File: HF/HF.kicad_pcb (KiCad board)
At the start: 2 copper layers, 105 x 58 mm, 11 parts, among them J1 SpeakON_NL4, J2 SpeakON_NL4, U1 1+, U2 1-, U3 HF-, U4 HF+

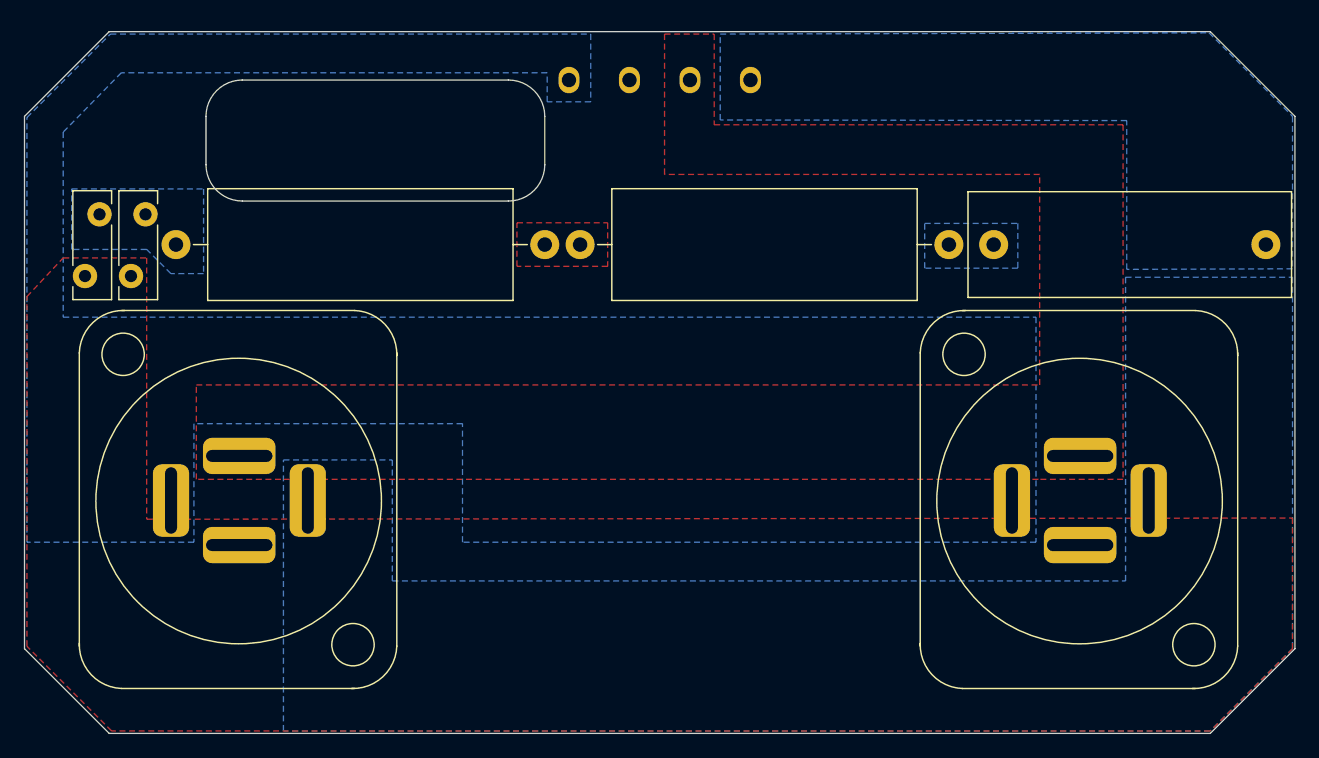
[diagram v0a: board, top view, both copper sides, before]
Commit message: added everything but the inductor
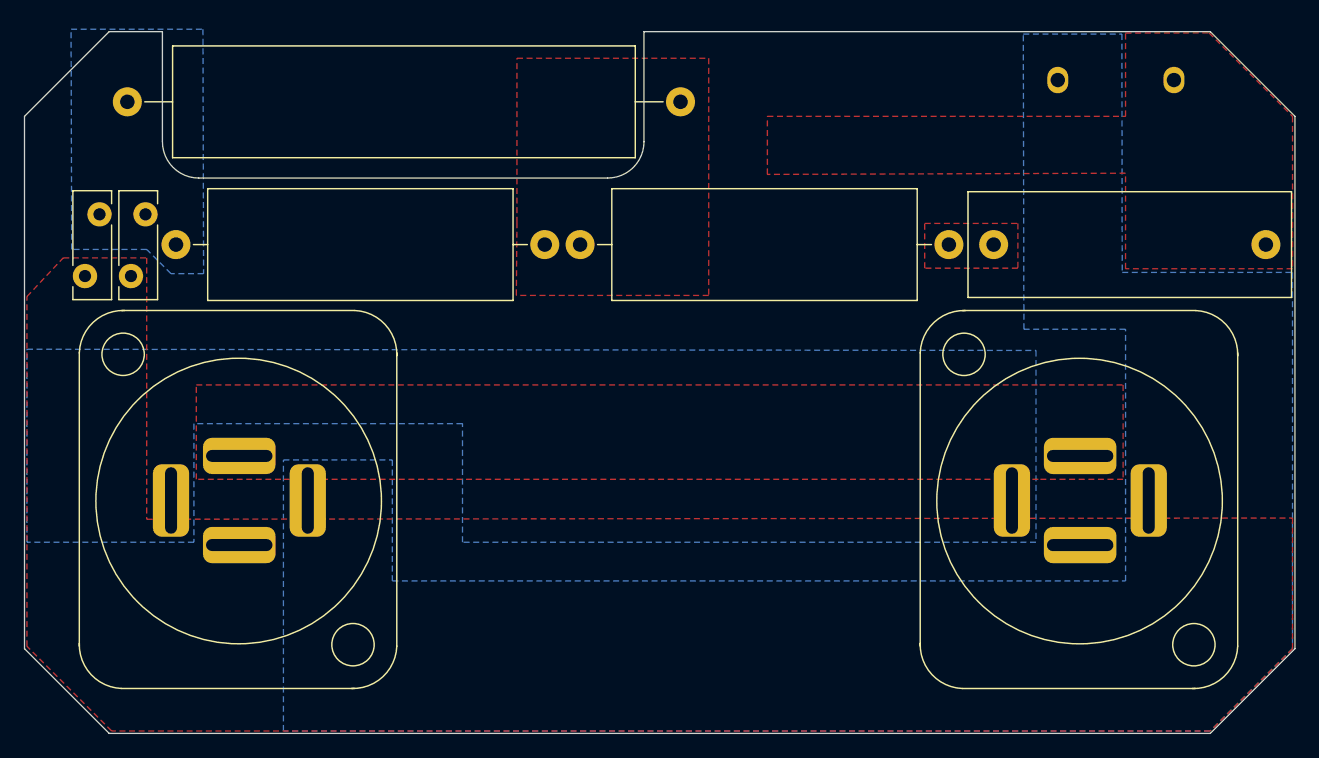
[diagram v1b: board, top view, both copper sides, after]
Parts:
- removed U1: 1+, SpeakON:Reoforo
- removed U2: 1-, SpeakON:Reoforo
- added LA1: 1,5Ω, Resistor_THT:R_Axial_Power_L38.0mm_W9.0mm_P45.72mm, F.Cu at (28.5, 25.8)
- moved U4 35.4 mm to (105.4, 24.0)
- moved U3 35.0 mm to (115.0, 24.0)
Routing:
- added copper zone on F.Cu, net Net-(C1-Pad1)
- added copper zone on F.Cu, net Net-(C1-Pad2)
- removed copper zone on B.Cu, net Net-(C1-Pad1)
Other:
- outline, holes or cut-outs redrawn

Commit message: inductor added
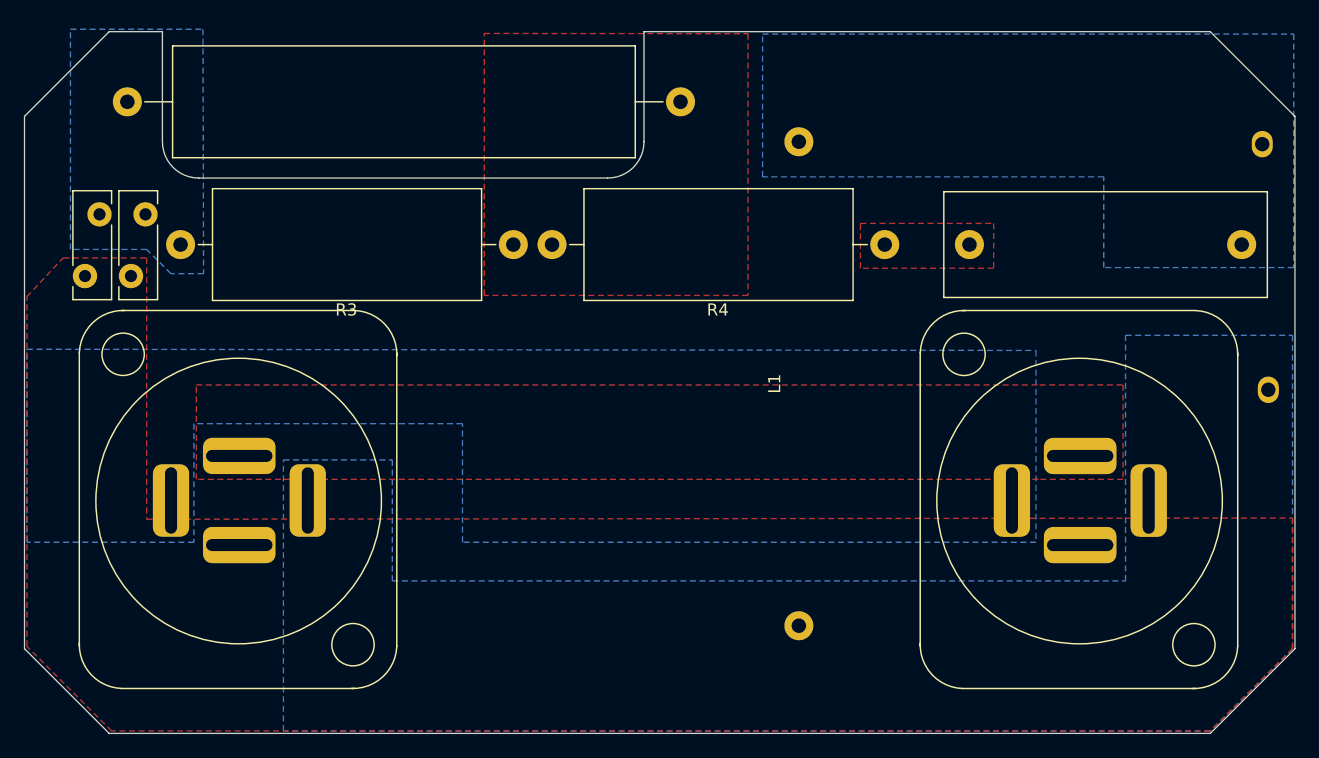
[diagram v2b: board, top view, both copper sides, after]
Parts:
- added L1: 290uH, RES:inductor_40mm, F.Cu at (80.0, 49.1)
- R3, R4: footprint Resistor_THT:R_Axial_Power_L25.0mm_W9.0mm_P30.48mm -> RES:resistor_P27.50mm
- moved U4 31.0 mm to (122.8, 49.6)
- moved U3 9.02 mm to (122.3, 29.3)
- moved R4 5.30 mm to (91.1, 37.6)
- moved R3 2.60 mm to (60.4, 37.6)
- moved C1 2.00 mm to (120.6, 37.6)
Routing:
- added copper zone on B.Cu, net Net-(C1-Pad1)
- removed copper zone on F.Cu, net Net-(C1-Pad1)

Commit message: updated speakON footprint
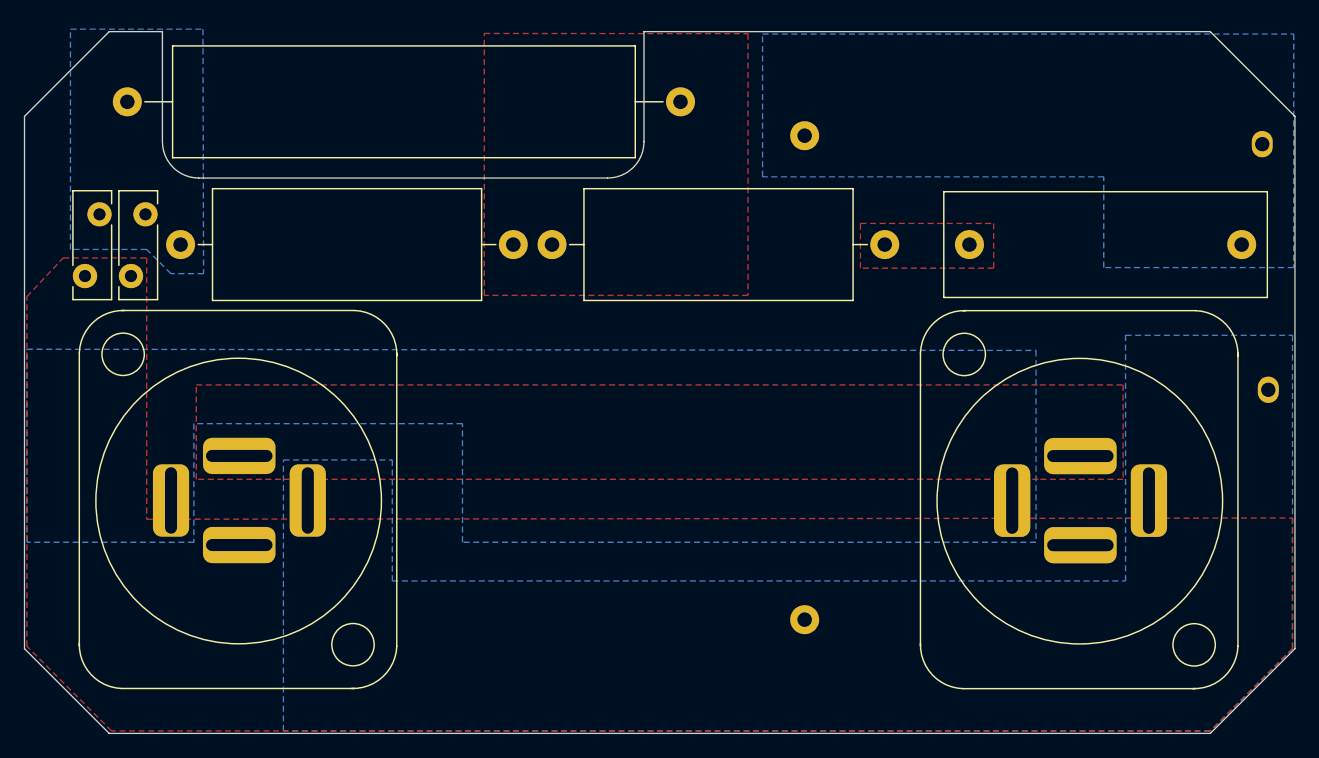
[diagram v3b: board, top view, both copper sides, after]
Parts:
- J1, J2: value SpeakON_NL4 -> NL4MP-M3
- moved L1 0.69 mm to (80.5, 48.6)
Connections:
- J1 pad 2-: Net-(C1-Pad2) -> Net-(J1-Pad2-)
- J2 pad 2-: Net-(C1-Pad2) -> Net-(J1-Pad2-)
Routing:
- added copper zone on B.Cu, net Net-(J1-Pad2-)
- removed copper zone on B.Cu, net Net-(C1-Pad2)

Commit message: changes from Trello
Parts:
- removed U3: HF-, SpeakON:Reoforo
- removed U4: HF+, SpeakON:Reoforo
- added G***: LOGO, PassiveFilters:fp02, B.Cu at (107.2, 37.6)
- added G***: LOGO, PassiveFilters:stakx_small_fp, B.Cu at (62.7, 70.7)
- added J3: Conn_01x02_Male, RES:Faston_DUAL_01x02_P5.08mm_D5.08mm, B.Cu at (79.8, 22.7)
- LA1: footprint Resistor_THT:R_Axial_Power_L38.0mm_W9.0mm_P45.72mm -> RES:lamp
- R1, R2: footprint Fuse:Fuse_Bourns_MF-RHT300 -> RES:ptc_7.2mm_larger
- moved L1 14.1 mm to (70.5, 58.6)
- moved C1 2.13 mm to (118.5, 37.6)
- moved R2 1.43 mm to (24.8, 35.5)
- moved R1 0.73 mm to (29.4, 35.5)
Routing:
- added copper zone on F.Cu, net Net-(C1-Pad1)
- added copper zone on B.Cu, net Net-(LA1-Pad2)
- removed copper zone on B.Cu, net Net-(C1-Pad1)
- removed copper zone on F.Cu, net Net-(LA1-Pad2)
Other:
- board text added: "+"
- board text added: "-"
- board text added: "1+"
- board text added: "1-"
- board text added: "2+"
- board text added: "JLCJLCJLCJLC"
- board text added: "MINISOUND HF"

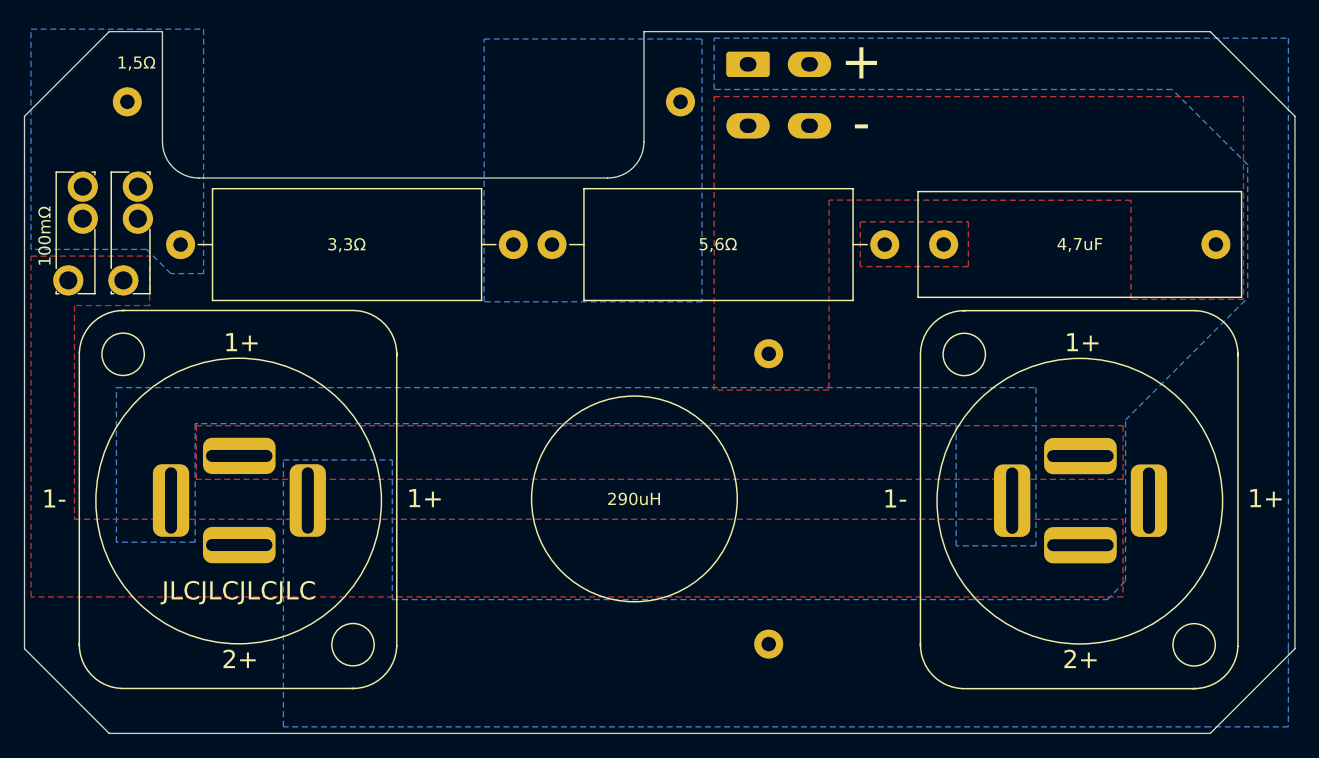
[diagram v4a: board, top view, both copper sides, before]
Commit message: added parallel board
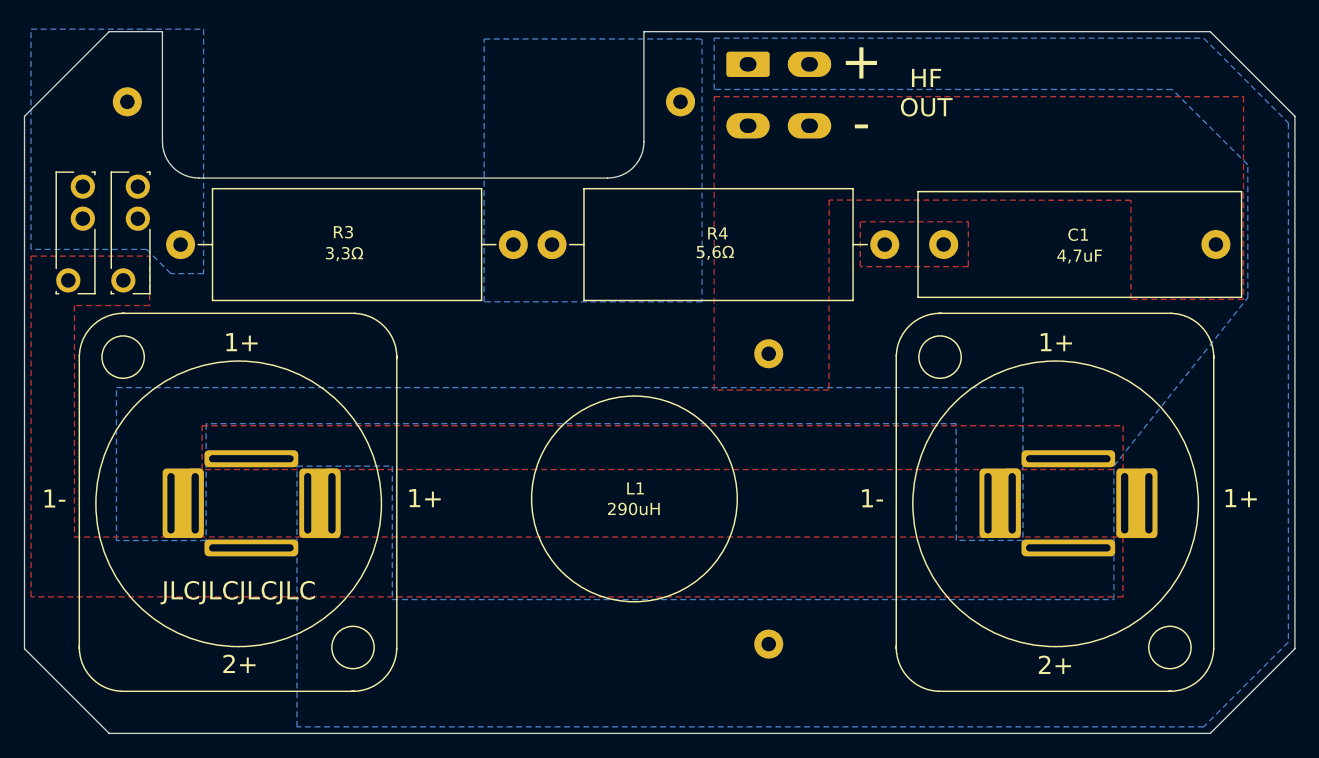
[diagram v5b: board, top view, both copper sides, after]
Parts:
- J1, J2: footprint SpeakON:NL4MP-M3 -> SpeakON:NL4MP-M3_double_left
- moved J2 2.01 mm to (105.3, 55.3)
- moved J1 0.23 mm to (37.8, 55.3)
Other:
- board text added: "HF OUT"
